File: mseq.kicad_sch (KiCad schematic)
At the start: 84 parts, among them J1 Screen_I2C, J3 Conn_ARM_JTAG_SWD_10, SW1 RESET, SW2 ON/OFF, SW3 MS/SLAVE, SW4 BOOT, U1 SN74AHCT125DR, U2 H11L1M, U3 MCP1703Ax-330xxTT, U4 STM32F413CHUx, U5 CP2102N-Axx-xQFN20, U6 H11L1M, U7 W25Q16JVSS, Y1 32.768kHz ±20ppm 6pF, Y2 25 MHz ±20ppm 18pF

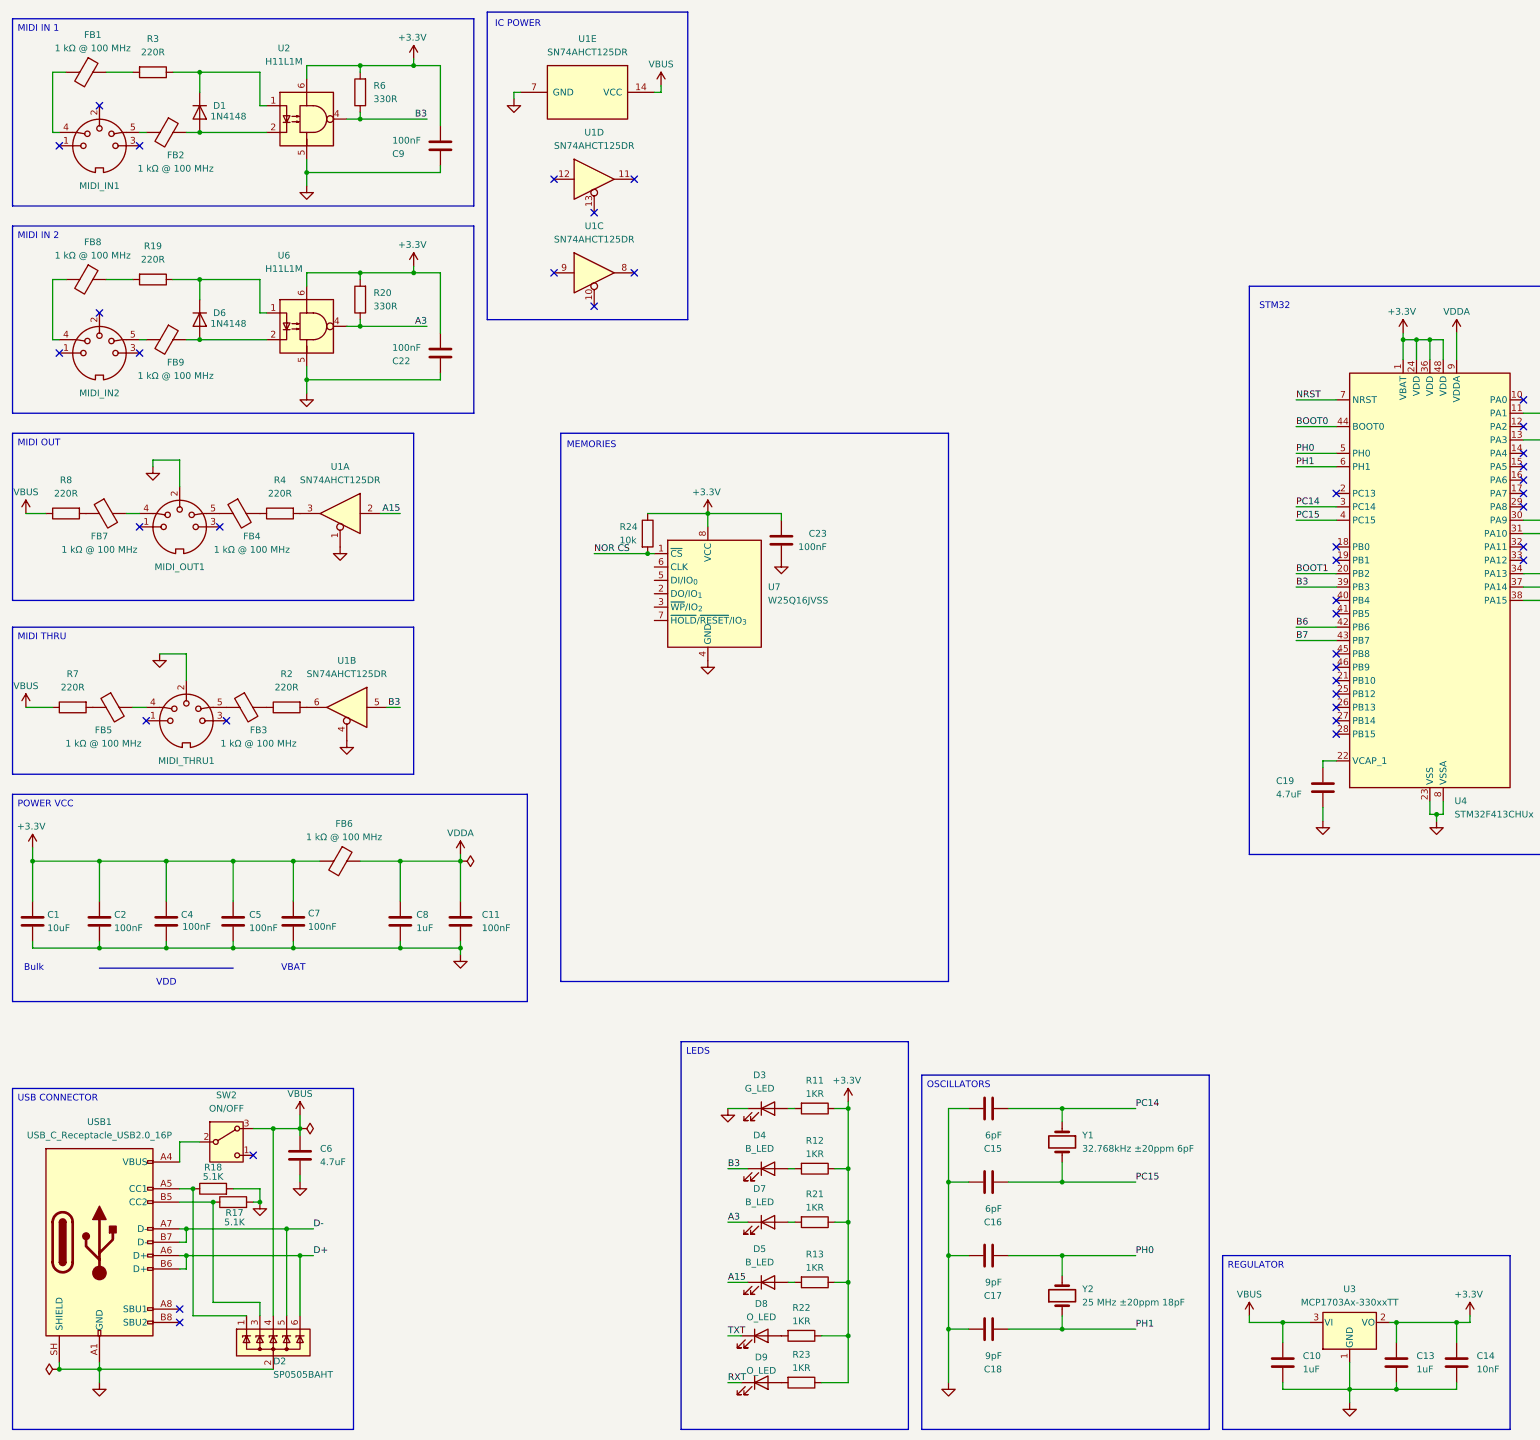
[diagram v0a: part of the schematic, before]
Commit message: SPI memories wired, AMS1117 regulator, schematic fixes
Add the NOR flash and FRAM to a shared SPI2 bus and clean up the
issues a full schematic review turned up.

Memories (U7 W25Q16JV, U8 MB85RS256B) share SCK/MOSI/MISO on
PB13/PB15/PB14 with separate chip selects on PB12 (NOR) and PB10
(FRAM), each with a 10k pull-up so both stay deselected through
reset. /WP and /HOLD tied high on both parts. QUADSPI is not
bonded out on the 48-pin STM32F413CHU6, so this is single SPI;
the FRAM sets the bus ceiling at 25 MHz for READ.

Regulator U3 moved from MCP1703A (SOT-23A) to AMS1117-3.3
(SOT-223). The SOT-23A's 336 C/W thermal resistance left almost
no margin at the ~166 mA peak load; SOT-223 removes the concern.
C13 accordingly goes 1uF -> 22uF and C10 1uF -> 10uF, since the
AMS1117 needs at least 10uF at VOUT for loop compensation where
the MCP1703A was stable from 1uF.

Also:
- Tie off U1 pins 9/10/12/13, the floating inputs on the two
  unused 74HCT125 buffer channels
- Correct U1 value to SN74HCT125DR to match the ordered part
- Assign missing footprints on U8, R17, R18; fill in BOM fields
- Exclude two ERC warnings on U7 /WP and /HOLD: the symbol
  declares them bidirectional for quad mode, unreachable here

ERC is clean: 0 errors, 0 warnings, 2 exclusions. PCB updated
from schematic; placement and routing not started.

Co-Authored-By: Claude Opus 5 <noreply@anthropic.com>
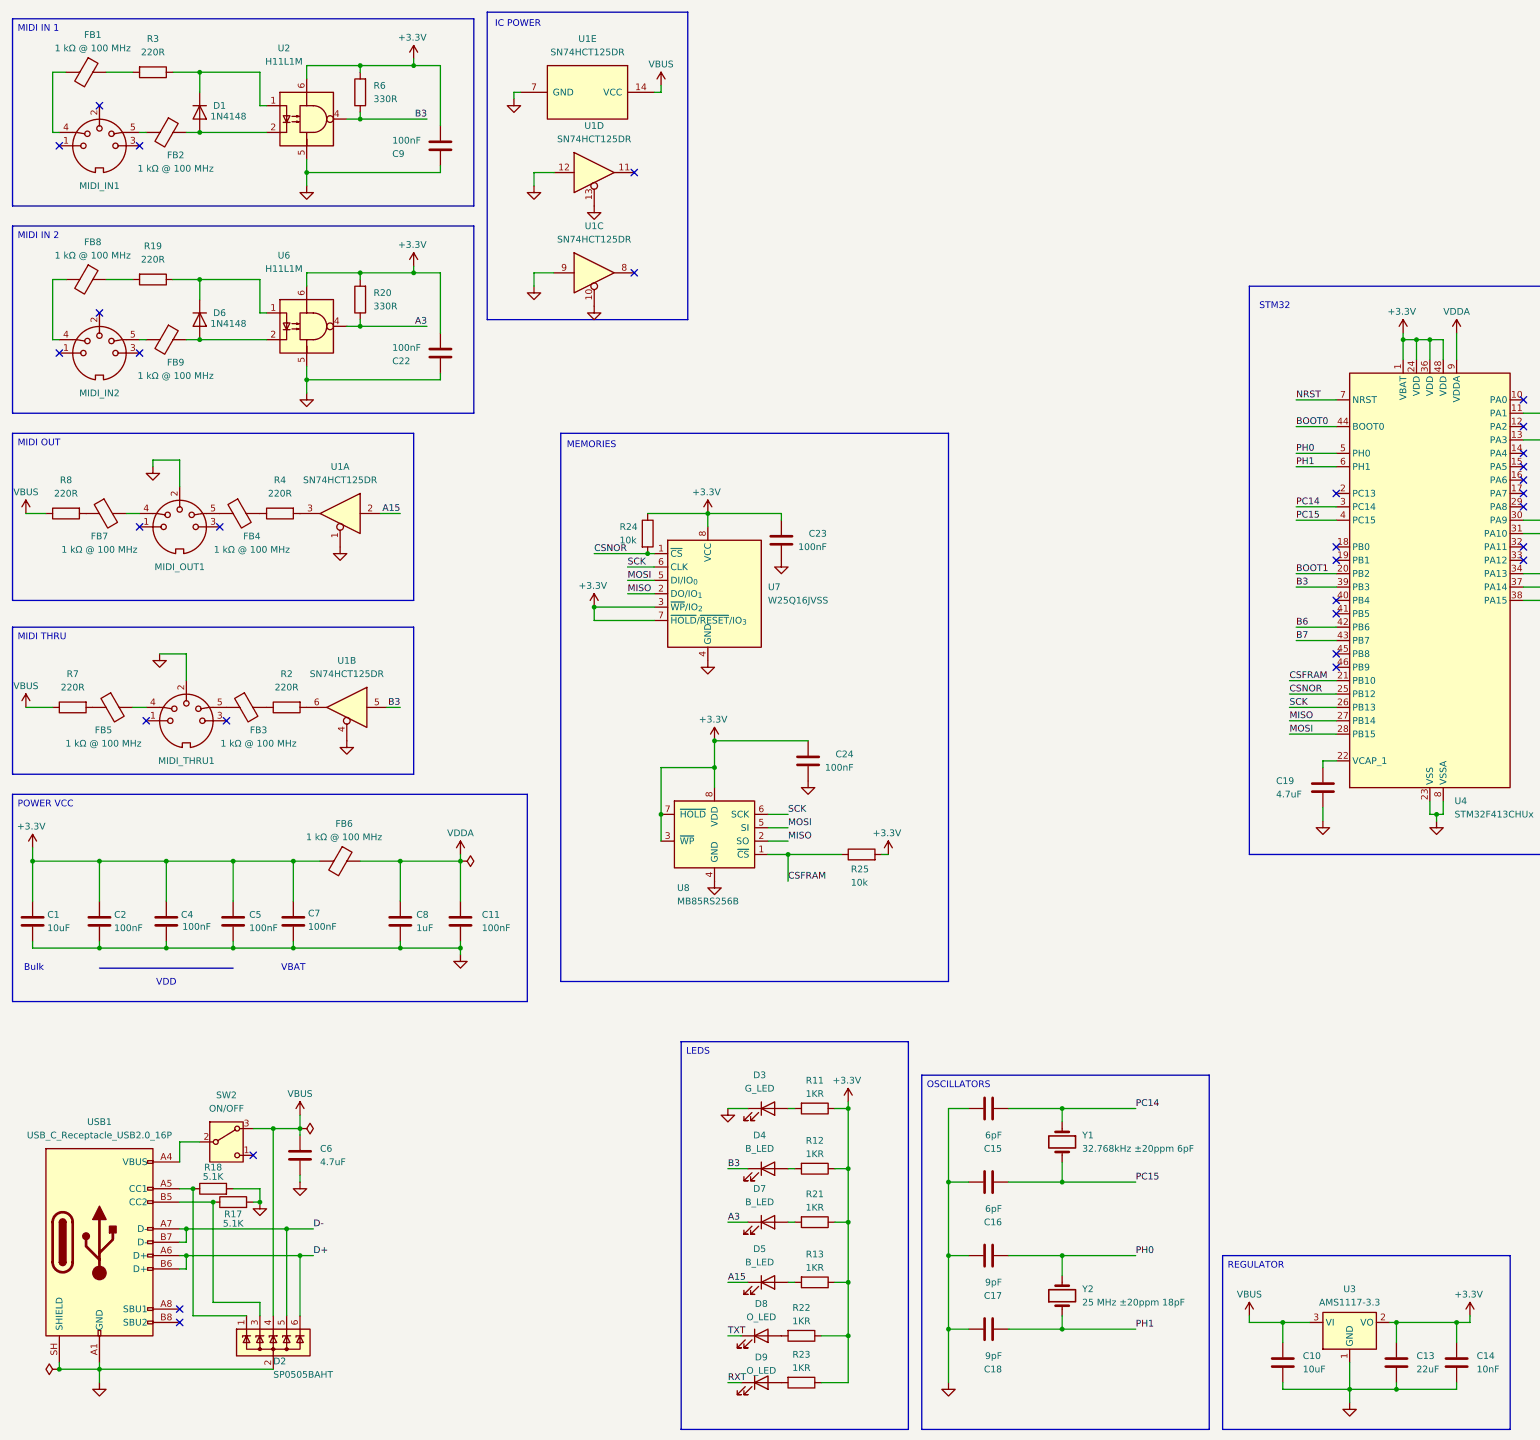
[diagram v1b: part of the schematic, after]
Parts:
- removed U3: MCP1703Ax-330xxTT, Package_TO_SOT_SMD:SOT-23, symbol Regulator_Linear:MCP1703Ax-330xxTT
- added C24: 100nF, Capacitor_SMD:C_0603_1608Metric, symbol Device:C
- added R25: 10k, Resistor_SMD:R_0603_1608Metric, symbol Device:R
- added U3: AMS1117-3.3, Package_TO_SOT_SMD:SOT-223-3_TabPin2, symbol Regulator_Linear:AMS1117-3.3
- added U8: MB85RS256B, Package_SO:SOIC-8_3.9x4.9mm_P1.27mm, symbol Memory_NVRAM:MB85RS256B
- C10: value 1uF -> 10uF; footprint Capacitor_SMD:C_0805_2012Metric -> Capacitor_SMD:C_1206_3216Metric; LCSC C1761 -> C14860; MPN CL21F105ZAFNNNE -> CL31B106KAHNNNE
- C13: value 1uF -> 22uF; footprint Capacitor_SMD:C_0805_2012Metric -> Capacitor_SMD:C_1206_3216Metric; LCSC C1761 -> C12891; MPN CL21F105ZAFNNNE -> CL31A226KAHNNNE
- J3: LCSC (none) -> C448647; MPN (none) -> FTSH-105-01-L-DV-K-TR
- R17, R18: footprint (none) -> Resistor_SMD:R_0603_1608Metric; LCSC (none) -> C23186; MPN (none) -> 0603WAF5101T5E
- U1: value SN74AHCT125DR -> SN74HCT125DR
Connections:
- net NOR CS is gone; now on net CSNOR: R24.2, U7.1 (~{CS})
- net +3.3V: now also U7.3 (~{WP}/IO_{2}), U7.7 (~{HOLD}/~{RESET}/IO_{3}), C24.2, R25.2, U3.2 (VO), U8.3 (~{WP}), U8.7 (~{HOLD}), U8.8 (VDD)
- net GND: now also U1.10, U1.12, U1.13, U1.9, C24.1, U3.1 (GND), U8.4 (GND)
- net VBUS: now also U3.3 (VI)
- net CSFRAM: now reaches U4.21 (PB10)
- net CSFRAM: now also R25.1, U8.1 (~{CS})
- net CSNOR: now reaches U4.25 (PB12)
- net SCK: now reaches U4.26 (PB13)
- net SCK: now also U7.6 (CLK), U8.6 (SCK)
- net MISO: now reaches U4.27 (PB14)
- net MISO: now also U7.2 (DO/IO_{1}), U8.2 (SO)
- net MOSI: now reaches U4.28 (PB15)
- net MOSI: now also U7.5 (DI/IO_{0}), U8.5 (SI)
- no-connect marks 49 -> 40
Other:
- moved on the sheet: U1D

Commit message: PCB placement & routing WIP, board logos, DRC exclusions
Add res/ with the MF Room square logo (dark background removed) and the
OSHW logo, both transparent SVGs ready for Import Graphics onto silkscreen.

Exclude the two text_thickness DRC warnings on the OFF and SLV silkscreen
labels. Not genuinely thin strokes: KiCad's FreeType conversion emits a
self-intersecting outline for Geist's F and L, so the DRC deflate test
collapses a degenerate sliver. Reproducible with those glyphs alone at any
size and weight, clean in Helvetica, and gone with a static Geist-Bold.ttf
in place of the variable font.

Also J1 MPN/LCSC filled in.

Co-Authored-By: Claude Opus 5 <noreply@anthropic.com>
Claude-Session: https://claude.ai/code/session_014D6qtQcTakGg9PCa4hkr3z
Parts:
- J1: LCSC C59481 -> C2718488; MPN (none) -> 2.54-1*4P
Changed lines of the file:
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@@
 			)
 		)
-		(property "LCSC" "C59481"
+		(property "LCSC" "C2718488"
 			(at 340.36 25.4 0)
 			(hide yes)
+			(show_name no)
+			(do_not_autoplace no)
+			(effects
+				(font
+					(size 1.27 1.27)
+				)
+			)
+		)
+		(property "MPN" "2.54-1*4P"
+			(at 340.36 25.4 0)
+			(hide yes)
